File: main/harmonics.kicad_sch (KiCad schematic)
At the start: 52 parts, among them SW1 SW_Rotary8, SW2 SW_Rotary8, SW3 SW_Rotary8, SW4 SW_SPDT, SW5 SW_SPDT, SW6 SW_SPDT, SW7 SW_SPDT, SW8 SW_Rotary8, U10 CD4017, U11 CD4017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

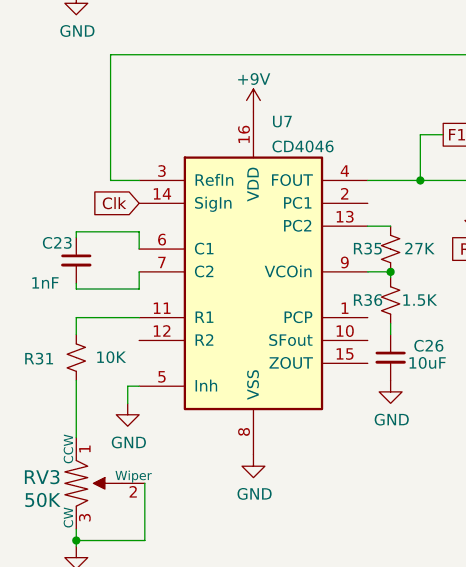
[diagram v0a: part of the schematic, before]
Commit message: Switched PLL cap to 680p
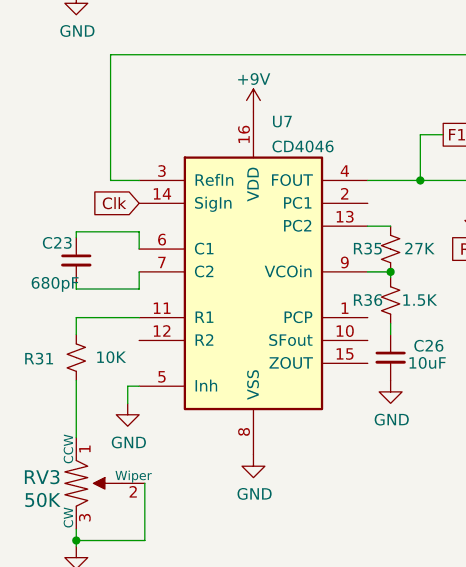
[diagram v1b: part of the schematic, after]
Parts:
- C23: value 1nF -> 680pF; LCSC Part # C46653 -> C384742
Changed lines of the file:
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@@
       (effects (font (size 1.27 1.27)) (justify left))
     )
-    (property "Value" "1nF" (id 1) (at 15.875 158.115 0)
+    (property "Value" "680pF" (id 1) (at 15.875 158.115 0)
       (effects (font (size 1.27 1.27)) (justify left))
     )
@@
       (effects (font (size 1.27 1.27)) hide)
     )
-    (property "LCSC Part #" "C46653" (id 5) (at 20.955 155.575 0)
+    (property "LCSC Part #" "C384742" (id 5) (at 20.955 155.575 0)
       (effects (font (size 1.27 1.27)) hide)
     )

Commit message: Switch to Thonk jacks.
Reduces use of extended parts.
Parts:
- U10, U11, U15, U9: LCSC Part # C11349 -> C356694
- U12, U13: footprint digikey-footprints:SOIC-14_W3.9mm -> Package_SO:SOIC-14_3.9x8.7mm_P1.27mm
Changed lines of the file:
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@@
       (effects (font (size 1.27 1.27)) (justify left))
     )
-    (property "Footprint" "digikey-footprints:SOIC-14_W3.9mm" (id 2) (at 137.16 88.265 0)
+    (property "Footprint" "Package_SO:SOIC-14_3.9x8.7mm_P1.27mm" (id 2) (at 137.16 88.265 0)
       (effects (font (size 1.27 1.27)) hide)
     )
@@
       (effects (font (size 1.27 1.27)) hide)
     )
-    (property "LCSC Part #" "C11349" (id 5) (at 80.645 40.64 0)
+    (property "LCSC Part #" "C356694" (id 5) (at 80.645 40.64 0)
       (effects (font (size 1.27 1.27)) hide)
     )
@@
       (effects (font (size 1.27 1.27)) (justify left))
     )
-    (property "Footprint" "digikey-footprints:SOIC-14_W3.9mm" (id 2) (at 137.16 33.02 0)
+    (property "Footprint" "Package_SO:SOIC-14_3.9x8.7mm_P1.27mm" (id 2) (at 137.16 33.02 0)
       (effects (font (size 1.27 1.27)) hide)
     )
@@
       (effects (font (size 1.27 1.27)) hide)
     )
-    (property "LCSC Part #" "C11349" (id 5) (at 238.125 40.64 0)
+    (property "LCSC Part #" "C356694" (id 5) (at 238.125 40.64 0)
       (effects (font (size 1.27 1.27)) hide)
     )
@@
       (effects (font (size 1.27 1.27)) (justify left))
     )
-    (property "Footprint" "digikey-footprints:SOIC-14_W3.9mm" (id 2) (at 221.615 88.9 0)
+    (property "Footprint" "Package_SO:SOIC-14_3.9x8.7mm_P1.27mm" (id 2) (at 221.615 88.9 0)
       (effects (font (size 1.27 1.27)) hide)
     )
@@
       (effects (font (size 1.27 1.27)) hide)
     )
-    (property "LCSC Part #" "C11349" (id 5) (at 80.01 159.385 0)
+    (property "LCSC Part #" "C356694" (id 5) (at 80.01 159.385 0)
       (effects (font (size 1.27 1.27)) hide)
     )
@@
       (effects (font (size 1.27 1.27)) (justify left))
     )
-    (property "Footprint" "digikey-footprints:SOIC-14_W3.9mm" (id 2) (at 137.16 149.225 0)
+    (property "Footprint" "Package_SO:SOIC-14_3.9x8.7mm_P1.27mm" (id 2) (at 137.16 149.225 0)
       (effects (font (size 1.27 1.27)) hide)
     )
@@
       (effects (font (size 1.27 1.27)) hide)
     )
-    (property "LCSC Part #" "C11349" (id 5) (at 80.01 99.06 0)
-      (effects (font (size 1.27 1.27)) hide)
-    )
+    (property "LCSC Part #" "C356694" (id 5) (at 80.01 99.06 0)
+      (effects (font (size 1.27 1.27)) hide)
+    )

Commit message: Version 1.0
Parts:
- added unit 3 of U12
- added unit 3 of U13
- RV2, RV3, RV4, RV5: footprint sputterizer:Potentiometer_Bourns_3224W_Vertical -> Potentiometer_SMD:Potentiometer_Bourns_3224W_Vertical
- U14, U6, U7, U8: Digi-Key Part (none) -> 296-32888-5-ND
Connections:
- net +9V: now also U12.14 (VDD), U13.14 (VDD); no longer U12.6 (S), U12.8 (S), U13.6 (S), U13.8 (S)
- net GND: now also U12.6 (S), U12.8 (S), U13.6 (S), U13.8 (S), U12.7 (VSS), U13.7 (VSS)

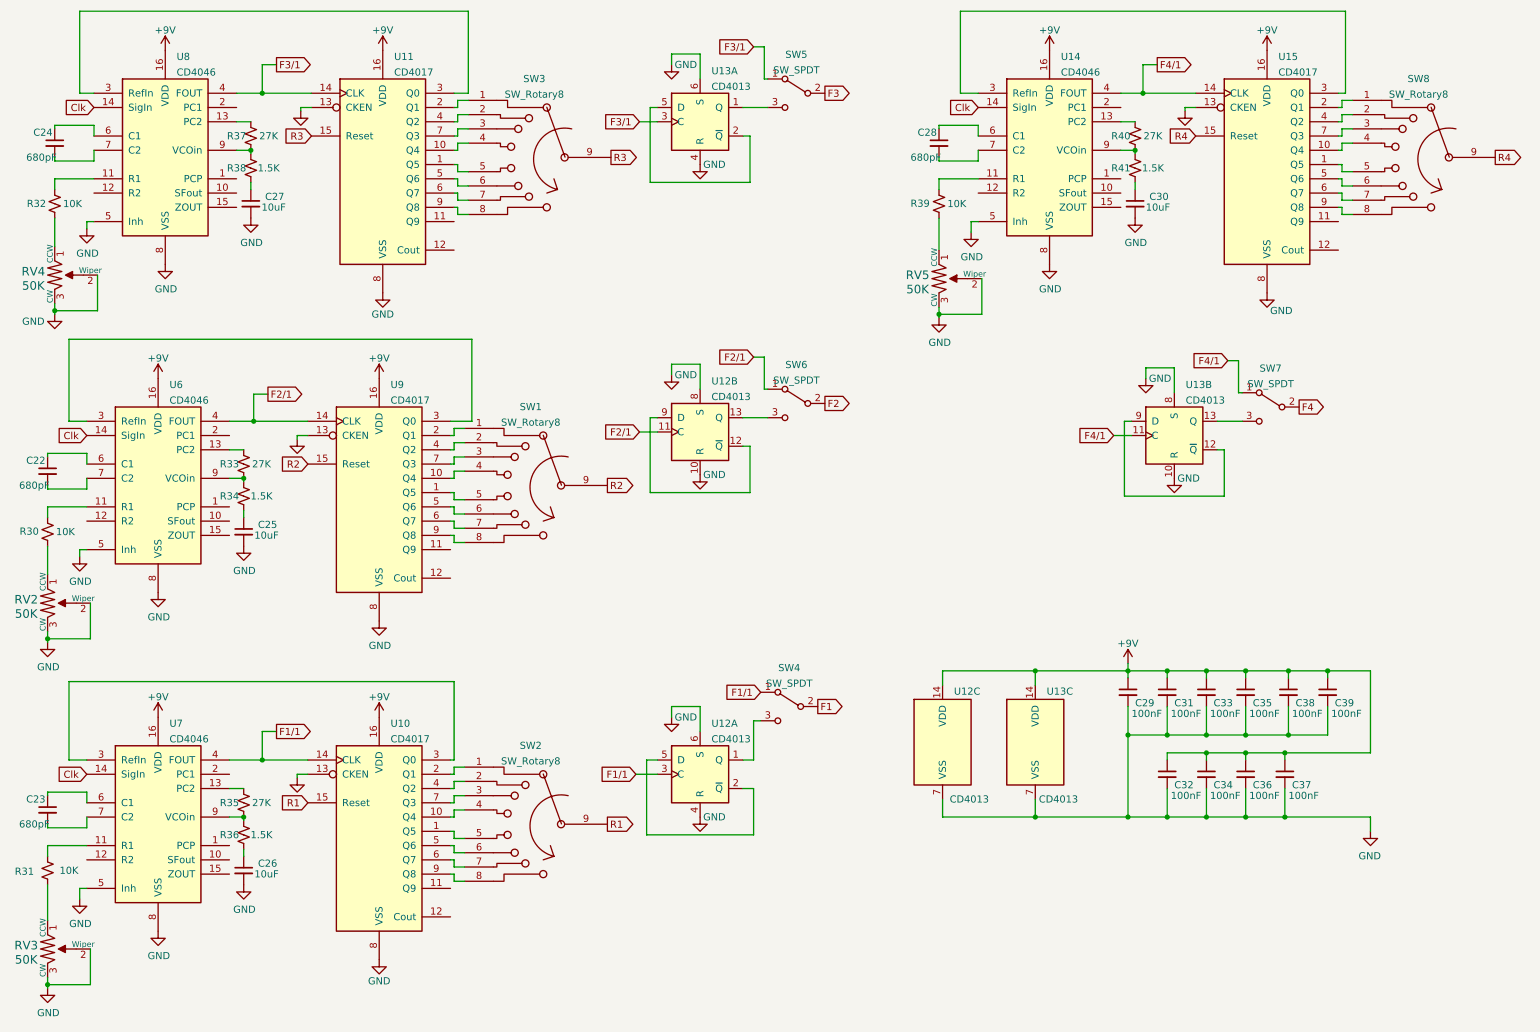
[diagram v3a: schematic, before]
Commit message: v1.0
Docs still need work.
Oscillators.sch not used. Saved just in case.
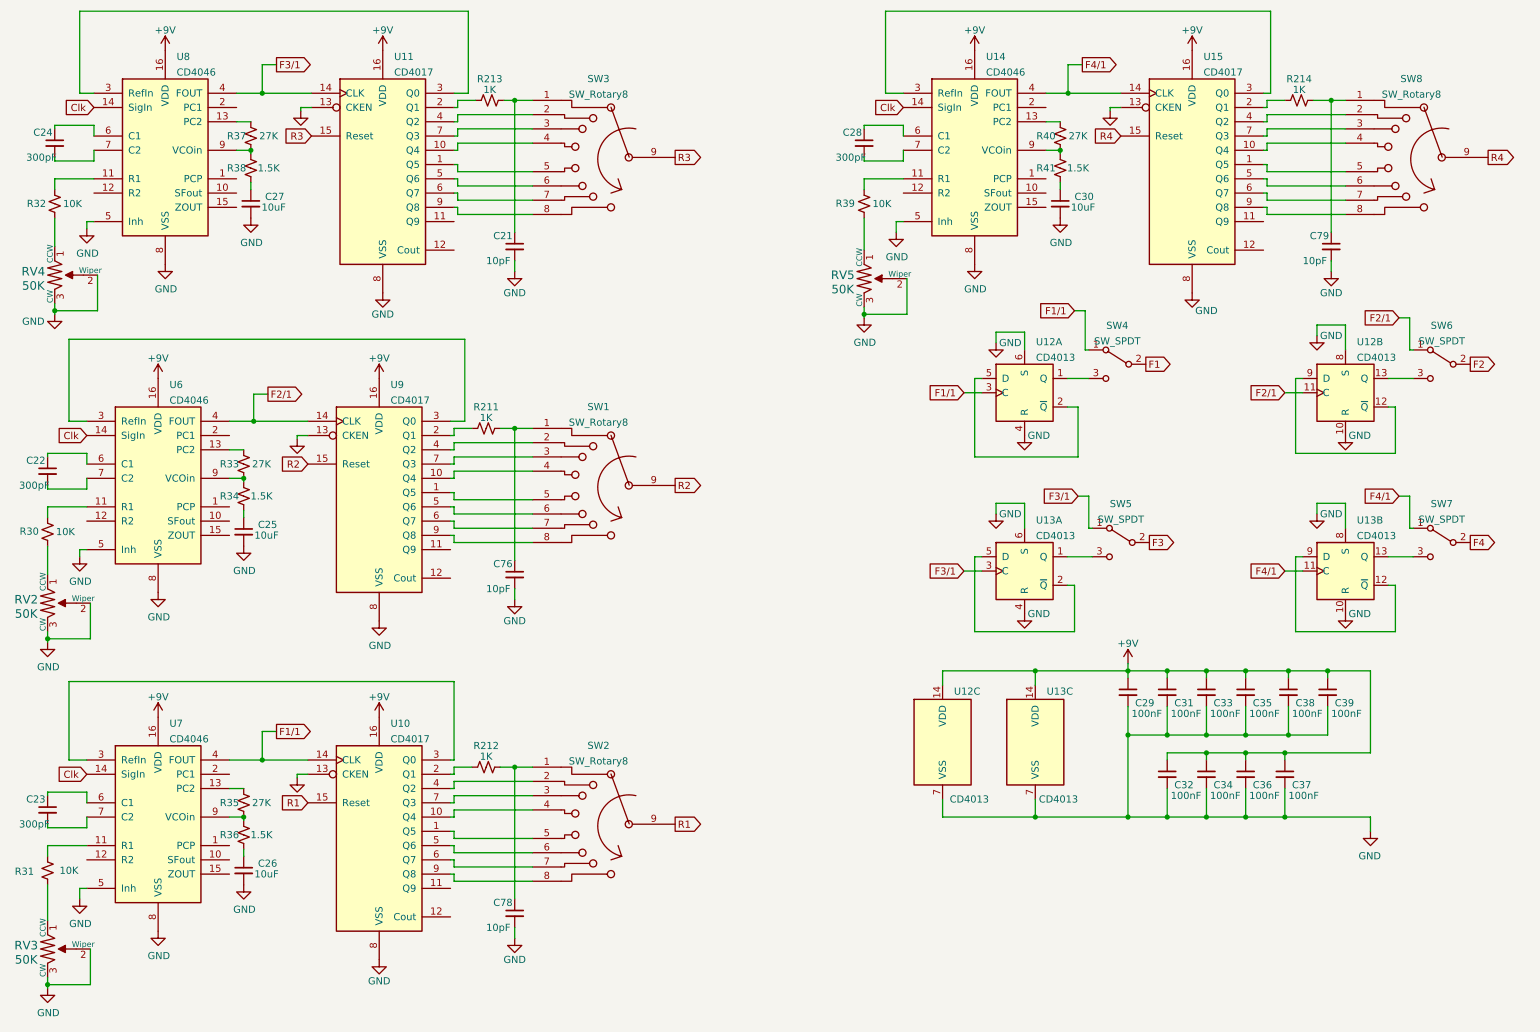
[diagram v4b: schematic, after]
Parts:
- added C21, C76, C78, C79: 10pF, Capacitor_SMD:C_0603_1608Metric_Pad1.08x0.95mm_HandSolder, symbol Device:C_Small
- added R211, R212, R213, R214: 1K, Resistor_SMD:R_0603_1608Metric, symbol Device:R_Small_US
- C22, C23, C24, C28: value 680pF -> 300pF; LCSC Part # C384742 -> C541567
- RV2, RV3, RV4, RV5: footprint Potentiometer_SMD:Potentiometer_Bourns_3224W_Vertical -> sputterizer:HDK_3mm; Digi-Key Part 490-2881-ND -> 118-TC33X-1-503ECT-ND; LCSC Part # C48484 -> C145161
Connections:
- net GND: now also C21.2, C76.2, C78.2, C79.2
- net at U11.2 (Q1): now also R213.2; no longer SW3.1
- net at SW1.1: now also C76.1, R211.1; no longer U9.2 (Q1)
- net at U15.2 (Q1): now also R214.2; no longer SW8.1
- net at SW2.1: now also C78.1, R212.1; no longer U10.2 (Q1)
- new net: R212.2, U10.2 (Q1)
- new net: R211.2, U9.2 (Q1)
- new net: C21.1, R213.1, SW3.1
- new net: C79.1, R214.1, SW8.1
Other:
- moved on the sheet: C28, C30, R39, R40, R41, RV5, SW1, SW2, SW3, SW4, SW5, SW6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

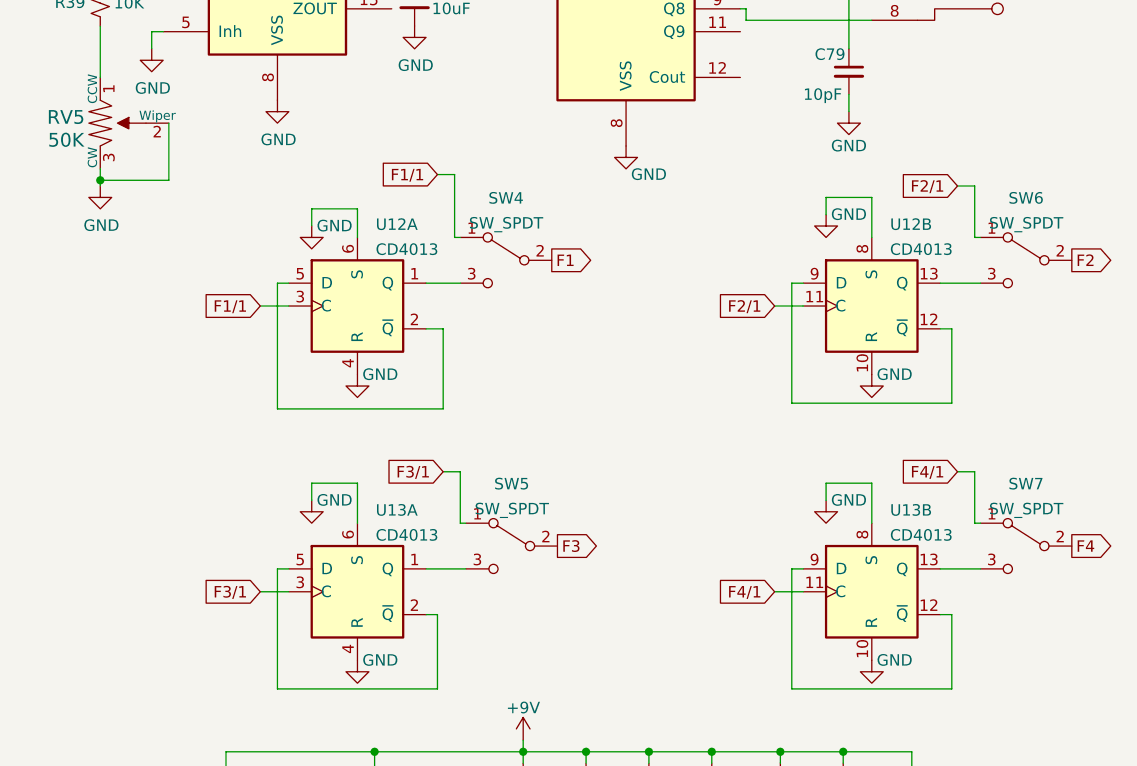
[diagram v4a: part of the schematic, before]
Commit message: Work in progress
Adds User Manual
Changes CV range to 0 - 8V
Adds spice vactrol test circuit.
Adds VCA spice study
Updates other spice and excel files.
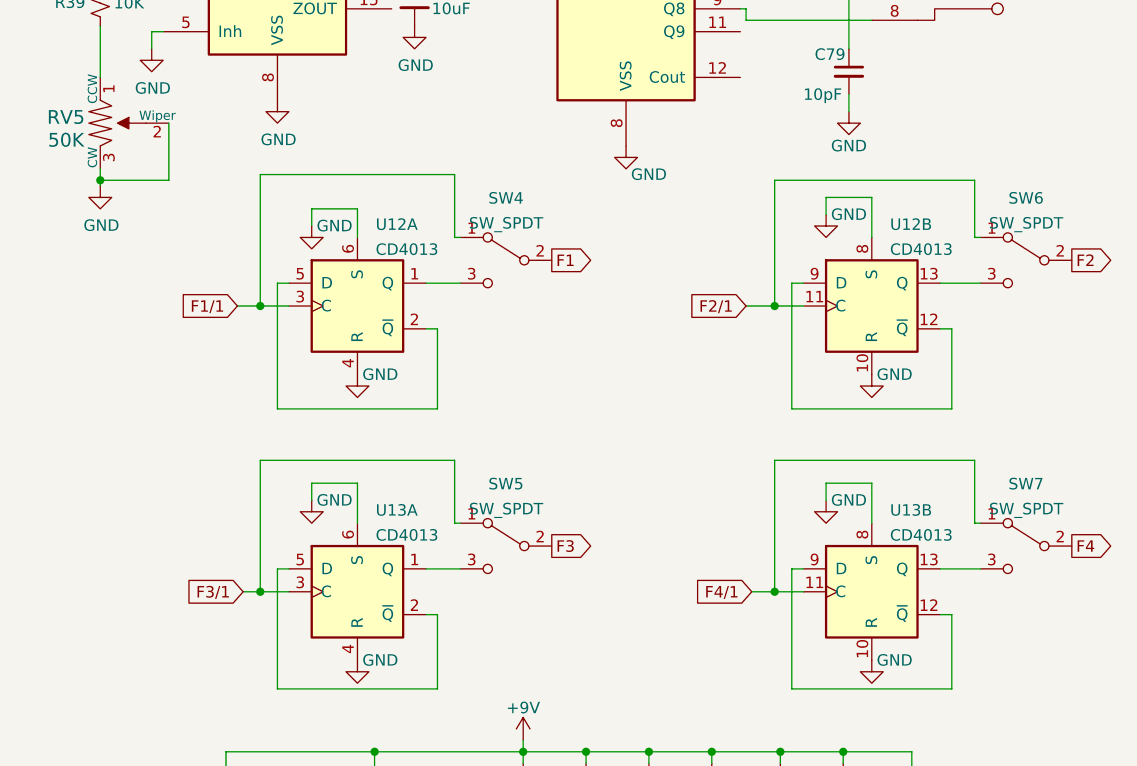
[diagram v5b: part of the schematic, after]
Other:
- title: (none) -> Twangilizer
- moved on the sheet: SW5

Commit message: Latest gain plan.
Version 1.1
Sent to JLCPCB
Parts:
- C22, C23, C24, C28: value 300pF -> 330pF; footprint Capacitor_SMD:C_0805_2012Metric_Pad1.18x1.45mm_HandSolder -> Capacitor_SMD:C_0603_1608Metric_Pad1.08x0.95mm_HandSolder; LCSC Part # C541567 -> C1664
- RV2, RV3, RV4, RV5: LCSC Part # C145161 -> C913246
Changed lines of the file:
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@@
       (effects (font (size 1.27 1.27)) (justify left))
     )
-    (property "Value" "300pF" (id 1) (at 15.875 158.115 0)
-      (effects (font (size 1.27 1.27)) (justify left))
-    )
-    (property "Footprint" "Capacitor_SMD:C_0805_2012Metric_Pad1.18x1.45mm_HandSolder" (id 2) (at 20.955 155.575 0)
+    (property "Value" "330pF" (id 1) (at 15.875 158.115 0)
+      (effects (font (size 1.27 1.27)) (justify left))
+    )
+    (property "Footprint" "Capacitor_SMD:C_0603_1608Metric_Pad1.08x0.95mm_HandSolder" (id 2) (at 20.955 155.575 0)
       (effects (font (size 1.27 1.27)) hide)
     )
@@
       (effects (font (size 1.27 1.27)) hide)
     )
-    (property "LCSC Part #" "C541567" (id 5) (at 20.955 155.575 0)
+    (property "LCSC Part #" "C1664" (id 5) (at 20.955 155.575 0)
       (effects (font (size 1.27 1.27)) hide)
     )
@@
       (effects (font (size 1.27 1.27)) (justify left))
     )
-    (property "Value" "300pF" (id 1) (at 17.145 39.37 0)
-      (effects (font (size 1.27 1.27)) (justify left))
-    )
-    (property "Footprint" "Capacitor_SMD:C_0805_2012Metric_Pad1.18x1.45mm_HandSolder" (id 2) (at 22.225 36.83 0)
+    (property "Value" "330pF" (id 1) (at 17.145 39.37 0)
+      (effects (font (size 1.27 1.27)) (justify left))
+    )
+    (property "Footprint" "Capacitor_SMD:C_0603_1608Metric_Pad1.08x0.95mm_HandSolder" (id 2) (at 22.225 36.83 0)
       (effects (font (size 1.27 1.27)) hide)
     )
@@
       (effects (font (size 1.27 1.27)) hide)
     )
-    (property "LCSC Part #" "C541567" (id 5) (at 22.225 36.83 0)
+    (property "LCSC Part #" "C1664" (id 5) (at 22.225 36.83 0)
       (effects (font (size 1.27 1.27)) hide)
     )
@@
       (effects (font (size 1.27 1.27)) hide)
     )
-    (property "LCSC Part #" "C145161" (id 6) (at 166.37 60.96 0)
+    (property "LCSC Part #" "C913246" (id 6) (at 166.37 60.96 0)
       (effects (font (size 1.27 1.27)) hide)
     )
@@
       (effects (font (size 1.27 1.27)) hide)
     )
-    (property "LCSC Part #" "C145161" (id 6) (at 20.955 180.34 0)
+    (property "LCSC Part #" "C913246" (id 6) (at 20.955 180.34 0)
       (effects (font (size 1.27 1.27)) hide)
     )
@@
       (effects (font (size 1.27 1.27)) (justify left))
     )
-    (property "Value" "300pF" (id 1) (at 161.29 39.37 0)
-      (effects (font (size 1.27 1.27)) (justify left))
-    )
-    (property "Footprint" "Capacitor_SMD:C_0805_2012Metric_Pad1.18x1.45mm_HandSolder" (id 2) (at 166.37 36.83 0)
+    (property "Value" "330pF" (id 1) (at 161.29 39.37 0)
+      (effects (font (size 1.27 1.27)) (justify left))
+    )
+    (property "Footprint" "Capacitor_SMD:C_0603_1608Metric_Pad1.08x0.95mm_HandSolder" (id 2) (at 166.37 36.83 0)
       (effects (font (size 1.27 1.27)) hide)
     )
@@
       (effects (font (size 1.27 1.27)) hide)
     )
-    (property "LCSC Part #" "C541567" (id 5) (at 166.37 36.83 0)
+    (property "LCSC Part #" "C1664" (id 5) (at 166.37 36.83 0)
       (effects (font (size 1.27 1.27)) hide)
     )
@@
       (effects (font (size 1.27 1.27)) (justify left))
     )
-    (property "Value" "300pF" (id 1) (at 15.875 97.79 0)
-      (effects (font (size 1.27 1.27)) (justify left))
-    )
-    (property "Footprint" "Capacitor_SMD:C_0805_2012Metric_Pad1.18x1.45mm_HandSolder" (id 2) (at 20.955 95.25 0)
+    (property "Value" "330pF" (id 1) (at 15.875 97.79 0)
+      (effects (font (size 1.27 1.27)) (justify left))
+    )
+    (property "Footprint" "Capacitor_SMD:C_0603_1608Metric_Pad1.08x0.95mm_HandSolder" (id 2) (at 20.955 95.25 0)
       (effects (font (size 1.27 1.27)) hide)
     )
@@
       (effects (font (size 1.27 1.27)) hide)
     )
-    (property "LCSC Part #" "C541567" (id 5) (at 20.955 95.25 0)
+    (property "LCSC Part #" "C1664" (id 5) (at 20.955 95.25 0)
       (effects (font (size 1.27 1.27)) hide)
     )
@@
       (effects (font (size 1.27 1.27)) hide)
     )
-    (property "LCSC Part #" "C145161" (id 6) (at 22.225 60.325 0)
+    (property "LCSC Part #" "C913246" (id 6) (at 22.225 60.325 0)
       (effects (font (size 1.27 1.27)) hide)
     )
@@
       (effects (font (size 1.27 1.27)) hide)
     )
-    (property "LCSC Part #" "C145161" (id 6) (at 20.955 118.745 0)
-      (effects (font (size 1.27 1.27)) hide)
-    )
+    (property "LCSC Part #" "C913246" (id 6) (at 20.955 118.745 0)
+      (effects (font (size 1.27 1.27)) hide)
+    )

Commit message: v2.0
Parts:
- RV2, RV3, RV4, RV5: footprint sputterizer:HDK_3mm -> greenface:Trimpot_3.8mmx3.6mm_TC33X-2-103E; symbol dk_Trimmer-Potentiometers:TC33X-2-103E -> greenface:TC33X-2-103E; Category (none) -> Potentiometers, Variable Resistors; DK_Datasheet_Link (none) -> https://www.bourns.com/docs/Product-Datasheets/TC33.pdf; DK_Detail_Page (none) -> /product-detail/en/bourns-inc/TC33X-2-103E/TC33X-103ETR-ND/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; Description_1 (none) -> TRIMMER 10K OHM 0.1W J LEAD TOP; Digi-Key_PN (none) -> TC33X-103ETR-ND; Family (none) -> Trimmer Potentiometers; MPN (none) -> TC33X-2-103E; Manufacturer (none) -> Bourns Inc.; Status (none) -> Active
- SW1, SW2, SW3, SW8: footprint sputterizer:CPA_8 -> greenface:CPA_8
- SW4, SW5, SW6, SW7: footprint digikey-footprints:Toggle_Switch_100SP1T1B4M2QE -> greenface:Toggle_Switch_100SP1T1B4M2QE
